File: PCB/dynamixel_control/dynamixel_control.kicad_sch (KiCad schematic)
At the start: 37 parts, among them J1 12V, J2 RS232, J6 Debug Uart, Q1 SSM3J372R, SW1 LIMIT_SWITCH, U1 R-78E5.0-0.5, U2 SN74AHC1G14, U3 LM810M3-4.63, U4 Teensy_4.0, U5 SN65C3221E, U6 ICM-40627

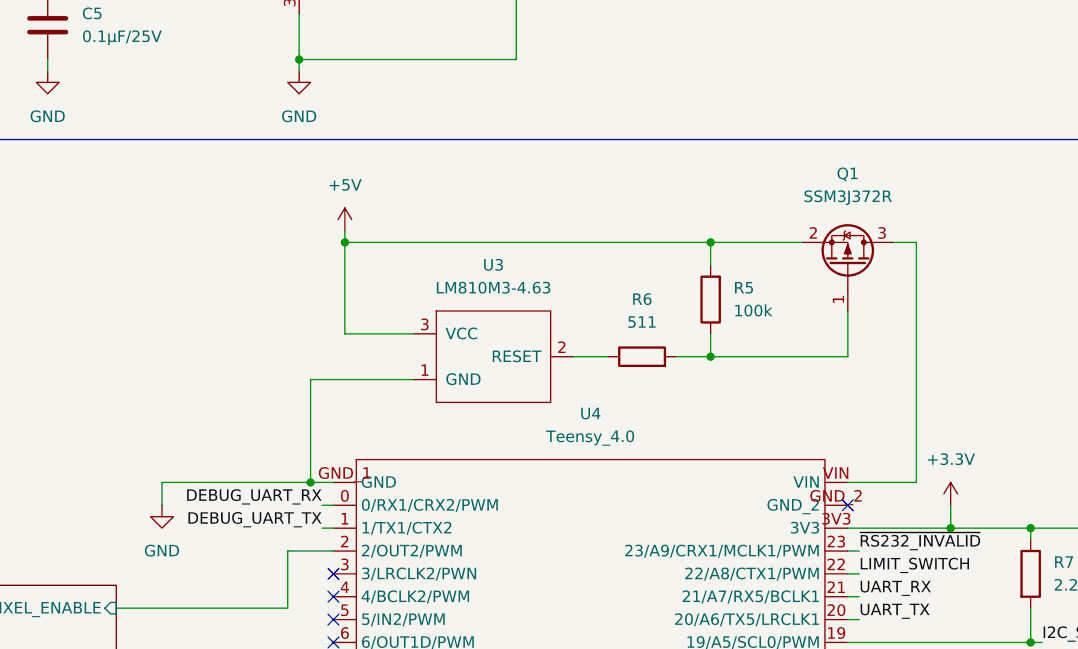
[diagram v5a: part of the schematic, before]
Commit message: Remove voltage supervisors
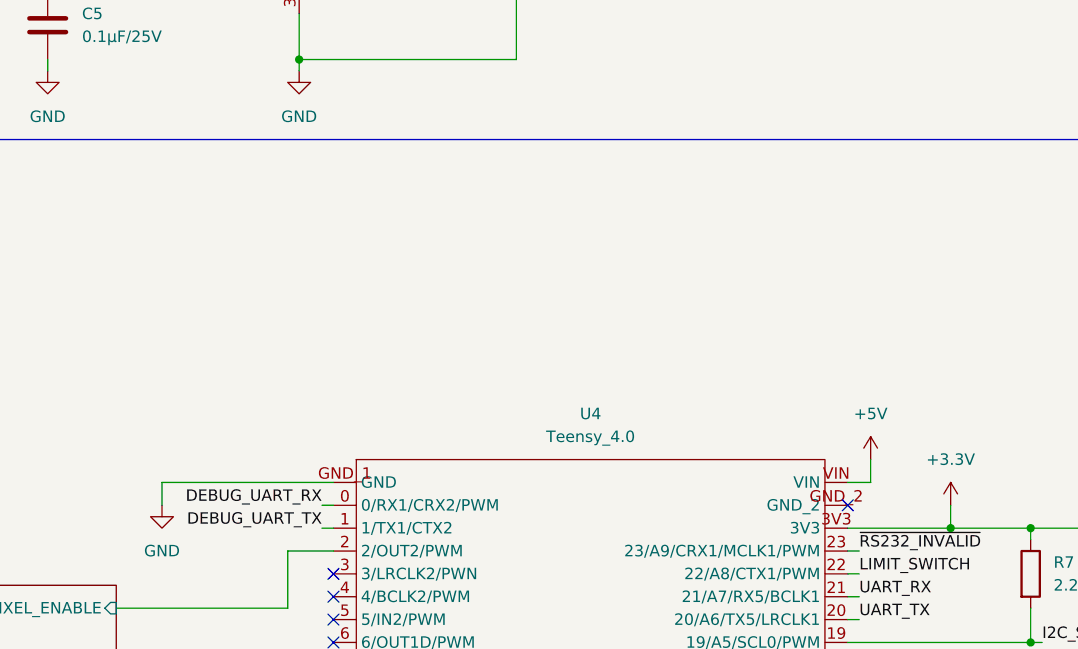
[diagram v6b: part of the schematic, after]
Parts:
- removed Q1: SSM3J372R, Package_TO_SOT_SMD:SOT-23, symbol Device:Q_PMOS_GSD
- removed R5: 100k, Resistor_SMD:R_0805_2012Metric, symbol Device:R
- removed R6: 511, Resistor_SMD:R_0805_2012Metric, symbol Device:R
- removed U3: LM810M3-4.63, Package_TO_SOT_SMD:SOT-23, symbol t-top:LM810
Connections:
- net +5V: now also U4.VIN
